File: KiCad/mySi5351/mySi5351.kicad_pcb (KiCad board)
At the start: 2 copper layers, 160 x 100 mm, 53 parts, among them J1 Conn_Coaxial, J10 Conn_01x01_Female, J2 Conn_Coaxial, J3 Conn_Coaxial, J4 Conn_Coaxial, J5 Conn_01x07_Female, J6 Conn_Coaxial, J7 Conn_01x01_Female, J8 Conn_01x02_Female, J9 Conn_01x05_Female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

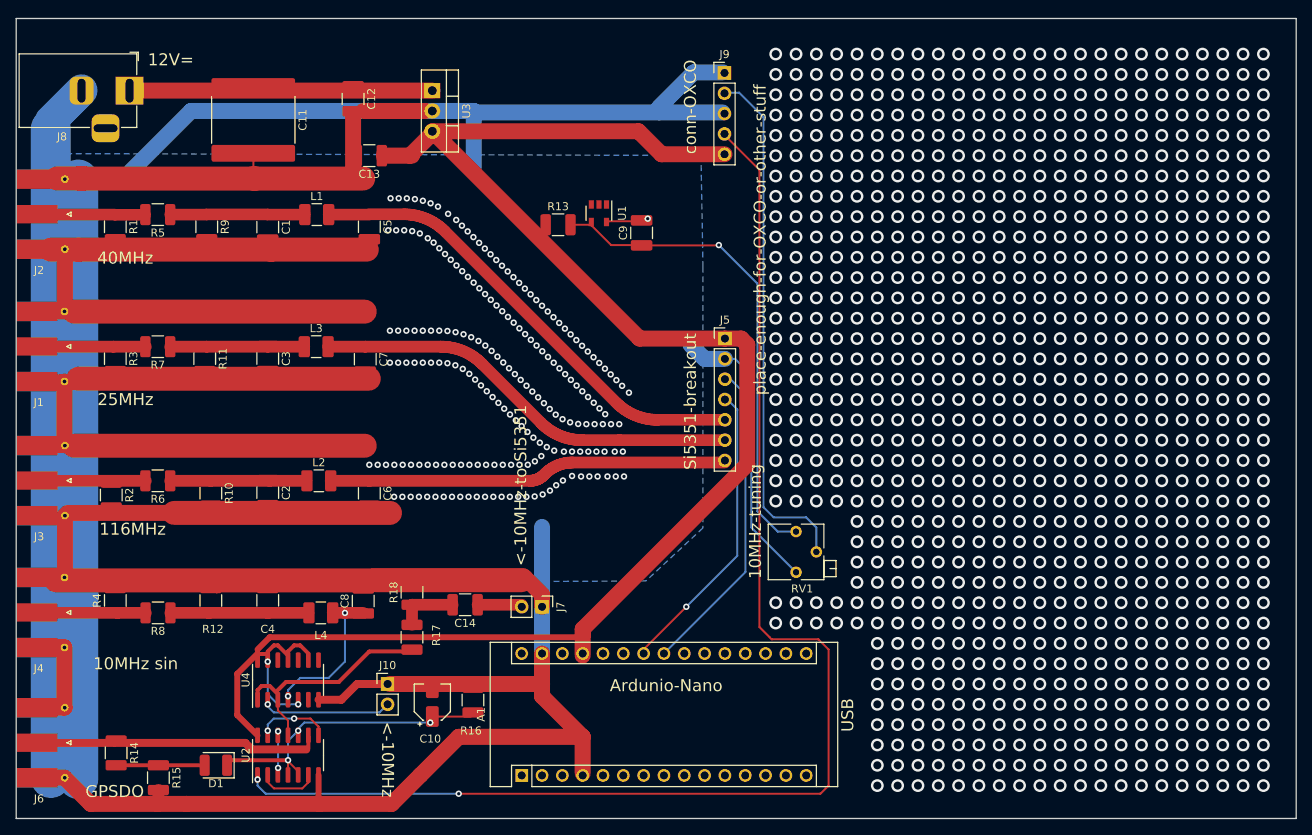
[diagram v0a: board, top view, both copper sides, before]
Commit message: Review, plotted files for first useable pcb
The plots are products and send to factory, not included in repo
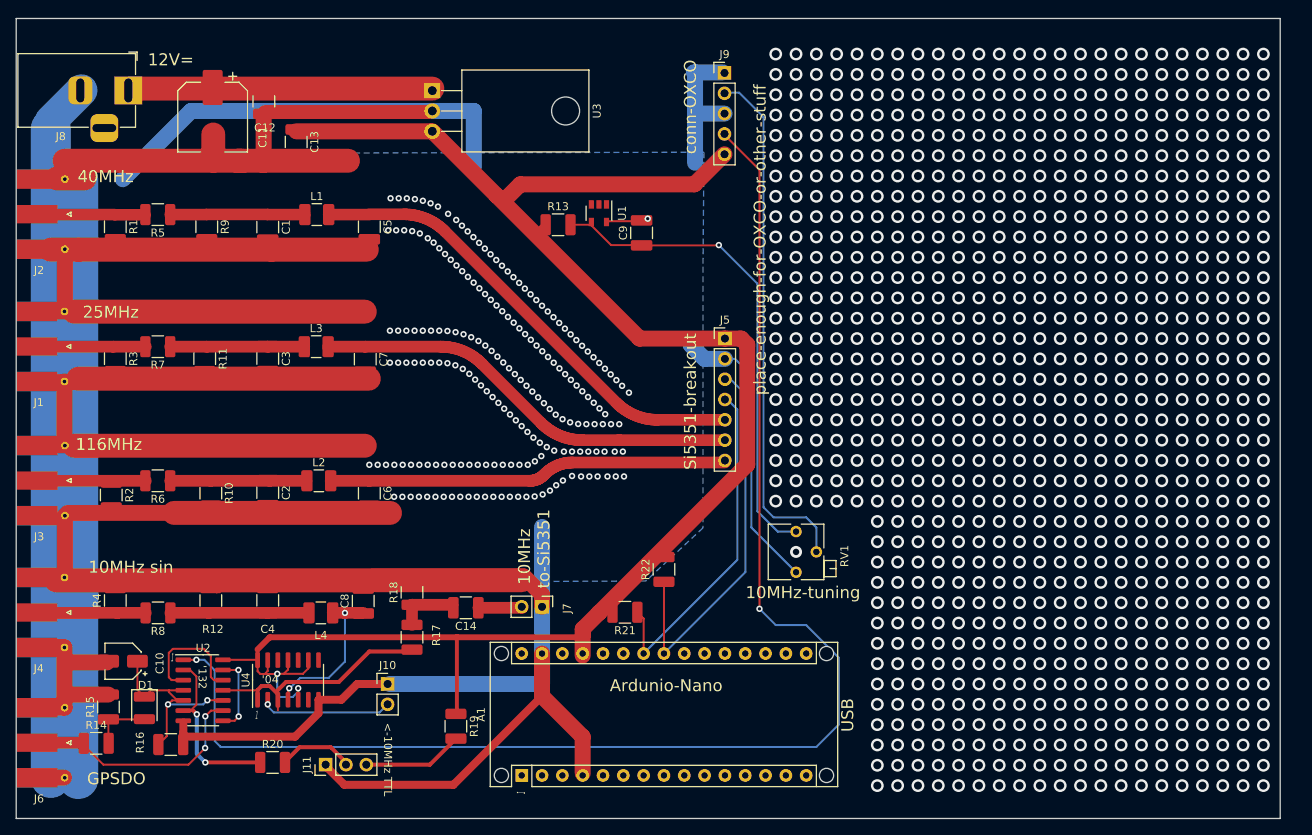
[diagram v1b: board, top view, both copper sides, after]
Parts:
- added J11: Conn_01x03_Female, Connector_PinHeader_2.54mm:PinHeader_1x03_P2.54mm_Vertical, F.Cu at (98.7, 133.3)
- added R19: 330, Resistor_SMD:R_1210_3225Metric_Pad1.30x2.65mm_HandSolder, F.Cu at (115.0, 128.5)
- added R20: 330, Resistor_SMD:R_1210_3225Metric_Pad1.30x2.65mm_HandSolder, F.Cu at (92.0, 133.0)
- added R21: 2k, Resistor_SMD:R_1210_3225Metric_Pad1.30x2.65mm_HandSolder, F.Cu at (136.1, 114.2)
- added R22: 2k, Resistor_SMD:R_1210_3225Metric_Pad1.30x2.65mm_HandSolder, F.Cu at (141.0, 108.9)
- added REF**: KiCad-Logo2_12mm_SilkScreen, Symbol:KiCad-Logo2_12mm_SilkScreen, B.Cu at (89.0, 69.6)
- added REF**: OSHW-Symbol_13.4x12mm_SilkScreen, Symbol:OSHW-Symbol_13.4x12mm_SilkScreen, B.Cu at (87.5, 90.5)
- A1: footprint Module:Arduino_Nano -> Module:Arduino_Nano_WithMountingHoles
- C11: footprint Capacitor_SMD:C_3640_9110Metric_Pad2.10x10.45mm_HandSolder -> Capacitor_SMD:CP_Elec_8x10.5
- U3: footprint Package_TO_SOT_THT:TO-220-3_Vertical -> Package_TO_SOT_THT:TO-220-3_Horizontal_TabDown
- moved C10 39.0 mm to (73.4, 120.3), turned to 180 degrees
- moved R16 38.2 mm to (79.3, 130.8), turned to 0 degrees
- moved U2 13.4 mm to (83.4, 124.0), turned to 0 degrees
- moved D1 11.5 mm to (76.0, 126.2), turned to 270 degrees
- moved C12 11.2 mm to (91.0, 50.4)
- moved R15 10.8 mm to (71.5, 126.1), turned to 90 degrees
- moved C13 9.30 mm to (95.0, 55.4), turned to 270 degrees
- moved C11 5.09 mm to (84.6, 52.3)
- moved R14 2.76 mm to (70.0, 130.6), turned to 0 degrees
- moved C14 0.39 mm to (116.2, 113.7)
- moved J8 0.15 mm to (74.0, 49.0)
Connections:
- net Net-(C11-Pad1) renamed PWR-Input
- net Net-(J10-Pad2) renamed 10MHz-TTL
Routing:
- net GND: track 812.6 -> 794.9 mm
- net Net-(R20-Pad1): track 8.38 -> 22.6 mm, vias 0 -> 2
- net Net-(C10-Pad1): track 40.2 -> 27.2 mm, vias 3 -> 2
- net Net-(J11-Pad3): track 0.00 -> 12.5 mm
- net OXCO-Output: track 163.4 -> 175.0 mm
- net Net-(U2-Pad12): track 4.57 -> 16.1 mm, vias 2 -> 0
- net Net-(J11-Pad2): track 0.00 -> 9.93 mm
- net SDA: track 40.7 -> 49.7 mm
- net +5V_Vcc: track 218.8 -> 227.0 mm
- net SCL: track 37.2 -> 42.9 mm, vias 1 -> 0
- net Net-(J6-Pad1): track 33.8 -> 29.6 mm, vias 0 -> 2
- net Net-(D1-Pad2): track 11.1 -> 7.51 mm
- net Net-(U2-Pad13): track 8.93 -> 10.0 mm
- net Net-(R17-Pad1): track 29.6 -> 30.3 mm
- net 10MHz-Out: track 19.3 -> 20.0 mm
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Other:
- board size 160 x 100 mm -> 158 x 100 mm
- board text added: "'04"
- board text added: "'132"
- board text added: "(c) 2020 DO1SLO"
- board text added: "1"
- board text added: "10MHz to-Si5351"
- board text added: "<-10MHz TTL"
- board text removed: "<-10MHz"
- board text removed: "<-10MHz-to-Si5351"
